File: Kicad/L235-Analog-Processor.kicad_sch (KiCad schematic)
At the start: 300 parts, among them J1 Input A, J10 Half Wave A + -B, J11 Inverted Out B, J12 CV Select, J13 CV Select, J14 Conn_01x20_Pin, J15 Inverted Out A, J16 Full-Wave Rectifier A, J17 Half-Wave Rectifier A, J18 √(A²+B²), J19 Conn_01x20_Socket, J2 Input B, J3 Function IN, J4 ( 10A / |B| ) / ( A * B / 10 ), J5 Output F(x), J6 Power, J7 Full-Wave Rectifier B, J8 A - B, J9 Negative Half-Wave Rectifier B, U1 TL082, U10 TL082, U11 TL082, U12 TL082, U13 TL084, U14 RC4580, U15 TL082, U16 AD633ARZ-RL, U17 TL082, U18 LM4040DBZ-10, U19 74HC148, U2 TL082, U20 LM339, U21 LM339, U22 DG4051E, U23 DG4051E, U24 DG4051E, U25 DG4051E, U26 DG4051E, U27 74LS151, U28 DG4051E, U29 LM339, U3 TL082, U30 LM339, U31 74HC148, U32 DG4051E, U33 DG4051E, U34 DG4051E, U35 DG4051E, U36 LM78M05_TO252, U37 TL082, U4 TL082, U5 TL082, U6 TL082, U7 TL082, U8 TL082, U9 TL082

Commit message: changed diode footprints to SOT-123
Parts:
- added C79, C83: 100nF, Capacitor_SMD:C_0402_1005Metric, symbol Device:C
- added U38: LM13700, symbol Amplifier_Operational:LM13700
- D1, D10, D11, D12, D13, D14, D15, D16, D17, D18, D19, D2, D20, D21, D22, D23, D25, D26, D29, D3, D30, D31, D32, D4, D5, D6, D7, D8, D9: footprint Diode_SMD:D_0402_1005Metric -> Diode_SMD:D_SOD-123
- R35, R37, R38, R82, R87, R88, R89, R91, R92, R93: value 180 -> 1k
- U22, U23, U24, U25, U26, U28: value DG4051E -> CD4051
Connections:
- net +12V: now also C79.1, U38.11 (V+)
- net -12V: now also C83.2, U38.6 (V-)
- net GND: now also TR2.4, C79.2, C83.1
- net at R33.2, RV3.1: no longer TR2.4

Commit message: Added test run
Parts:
- U27: value 74LS151 -> CD4051
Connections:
- net 10V REF is gone; now on net +5V: C43.2, J1.TN, J14.14 (Pin_14), J19.14 (Pin_14), J2.TN, R110.2, R16.2, R2.2, R65.2, R98.2, U18.1 (K)
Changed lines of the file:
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@@
     )
   )
+  (symbol (lib_id "power:+5V") (at 38.1 467.36 0) (unit 1)
+    (in_bom yes) (on_board yes) (dnp no) (fields_autoplaced)
+    (property "Reference" "#PWR0187" (at 38.1 471.17 0)
+      (effects (font (size 1.27 1.27)) hide)
+    )
+    (property "Value" "+5V" (at 38.1 462.28 0)
+      (effects (font (size 1.27 1.27)))
+    )
+    (property "Footprint" "" (at 38.1 467.36 0)
+      (effects (font (size 1.27 1.27)) hide)
+    )
+    (property "Datasheet" "" (at 38.1 467.36 0)
+      (effects (font (size 1.27 1.27)) hide)
+    )
+    (pin "1")
+    (instances
+      (project "L235-Analog-Processor"
+        (path "/11565f7a-671a-4a91-8d3b-c6d6401f938b"
+          (reference "#PWR0187") (unit 1)
+        )
+      )
+    )
+  )
   (symbol (lib_id "Amplifier_Operational:TL082") (at 101.473 266.319 0) (mirror x) (unit 2)
     (in_bom yes) (on_board yes) (dnp no)
@@
       (effects (font (size 1.27 1.27)))
     )
-    (property "Value" "74LS151" (at 181.61 845.9821 0)
+    (property "Value" "CD4051" (at 181.61 845.9821 0)
       (effects (font (size 1.27 1.27)))
     )

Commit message: Added leds selectors
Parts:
- removed H2: MountingHole, MountingHole:MountingHole_3.2mm_M3_DIN965, symbol Mechanical:MountingHole
- added C84, C85, C86, C87: 100nF, Capacitor_SMD:C_0402_1005Metric, symbol Device:C
- added D27, D28, D35, D36, D37, D38, D39, D40, D41, D42, D43, D44, D45: LED, LED_THT:LED_D1.8mm_W3.3mm_H2.4mm, symbol Device:LED
- added J20, J22: Conn_01x05_Socket, Connector_PinHeader_2.54mm:PinHeader_1x05_P2.54mm_Vertical, symbol Connector:Conn_01x05_Socket
- added J21, J23: Conn_01x05_Pin, Connector_PinSocket_2.54mm:PinSocket_1x05_P2.54mm_Vertical, symbol Connector:Conn_01x05_Pin
- added R115, R55: 1k, Resistor_SMD:R_0402_1005Metric, symbol Device:R
- added U39, U40: CD4051, Package_SO:TSSOP-16-1EP_4.4x5mm_P0.65mm_EP3x3mm, symbol 4xxx:4051
- RV7: value 500k -> 1M Log
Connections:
- net +12V: now also C84.2, C87.2, U39.16 (VDD), U40.16 (VDD)
- net +5V: now also J20.5 (Pin_5), J21.5 (Pin_5), J22.5 (Pin_5), J23.5 (Pin_5), R115.1, R55.1; no longer C43.2, J1.TN, J14.14 (Pin_14), J19.14 (Pin_14), J2.TN, R2.2, U18.1 (K)
- net -12V: now also C85.2, C86.2, U39.8 (VSS), U40.8 (VSS)
- net A0: now also J20.2 (Pin_2), J21.2 (Pin_2), U39.11 (A)
- net A1: now also J20.3 (Pin_3), J21.3 (Pin_3), U39.10 (B)
- net A2: now also J20.4 (Pin_4), J21.4 (Pin_4), U39.9 (C)
- net B0: now also J22.2 (Pin_2), J23.2 (Pin_2), U40.11 (A)
- net B1: now also J22.3 (Pin_3), J23.3 (Pin_3), U40.10 (B)
- net B2: now also J22.4 (Pin_4), J23.4 (Pin_4), U40.9 (C)
- net GND: now also C84.1, C85.1, C86.1, C87.1, D27.1 (K), D28.1 (K), D35.1 (K), D36.1 (K), D37.1 (K), D38.1 (K), D39.1 (K), D40.1 (K), D41.1 (K), D42.1 (K), D43.1 (K), D44.1 (K), D45.1 (K), J20.1 (Pin_1), J21.1 (Pin_1), J22.1 (Pin_1), J23.1 (Pin_1), U39.6 (Inh), U39.7 (VEE), U40.6 (Inh), U40.7 (VEE)
- new net: R55.2, U40.3 (X)
- new net: R115.2, U39.3 (X)
- new net 10V REF: C43.2, J1.TN, J14.14 (Pin_14), J19.14 (Pin_14), J2.TN, R2.2, U18.1 (K)
- new net LED_A1: D27.2 (A), U39.13 (X0)
- new net LED_A2: D28.2 (A), U39.14 (X1)
- new net LED_A3: D35.2 (A), U39.15 (X2)
- new net LED_A4: D39.2 (A), U39.12 (X3)
- new net LED_A5: D38.2 (A), U39.1 (X4)
- new net LED_A6: D37.2 (A), U39.5 (X5)
- new net LED_A7: D36.2 (A), U39.2 (X6)
- new net LED_B1: D40.2 (A), U40.13 (X0)
- new net LED_B2: D41.2 (A), U40.14 (X1)
- new net LED_B3: D42.2 (A), U40.15 (X2)
- new net LED_B4: D43.2 (A), U40.12 (X3)
- new net LED_B5: D44.2 (A), U40.1 (X4)
- new net LED_B6: D45.2 (A), U40.5 (X5)
- no-connect marks 52 -> 55
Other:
- note added: "( 10A / |B| ) / ( A * B / 10 )"
- note added: "A"
- note added: "B"
- note added: "Integrator"
- note added: "Negative"
- note added: "ln |X| / √|X| / X²"

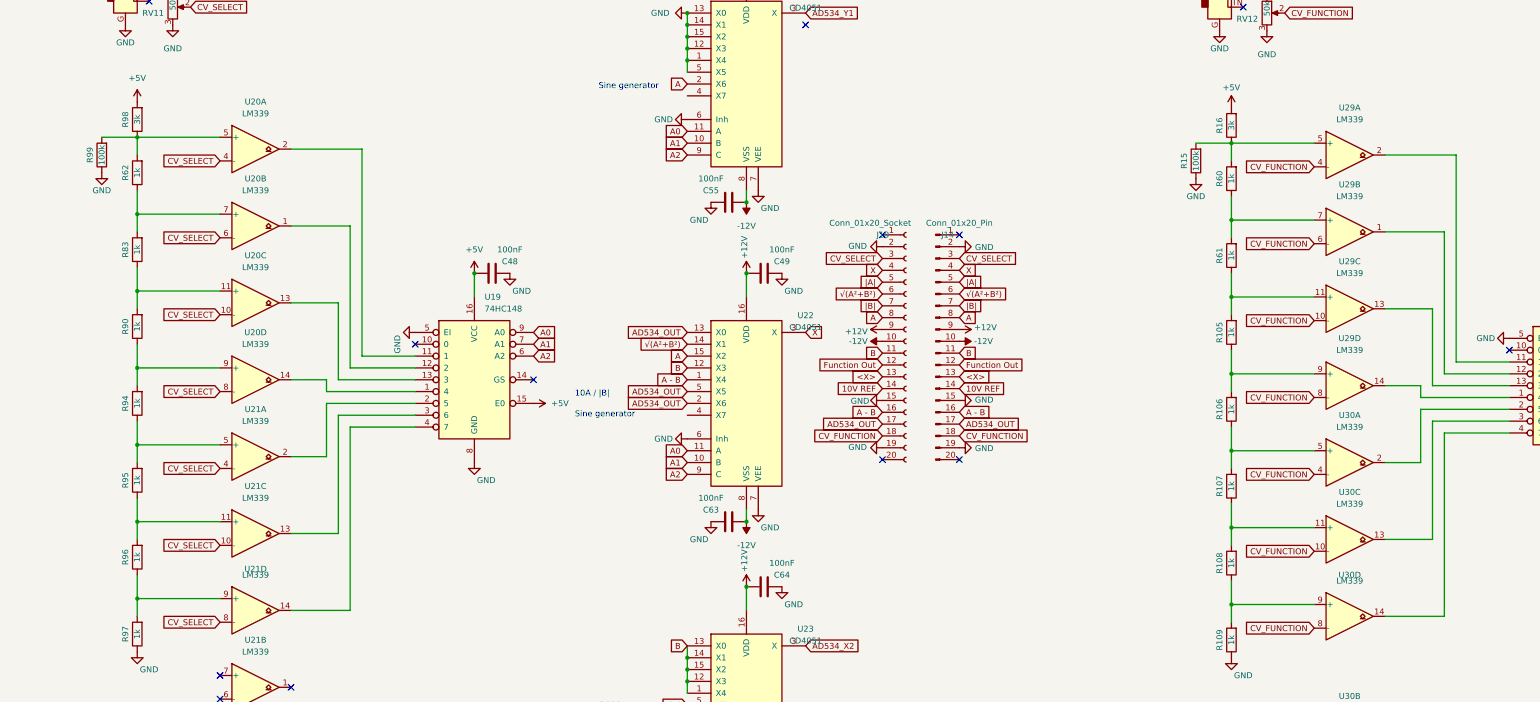
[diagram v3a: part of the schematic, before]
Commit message: Added missing Vlogic to comparators
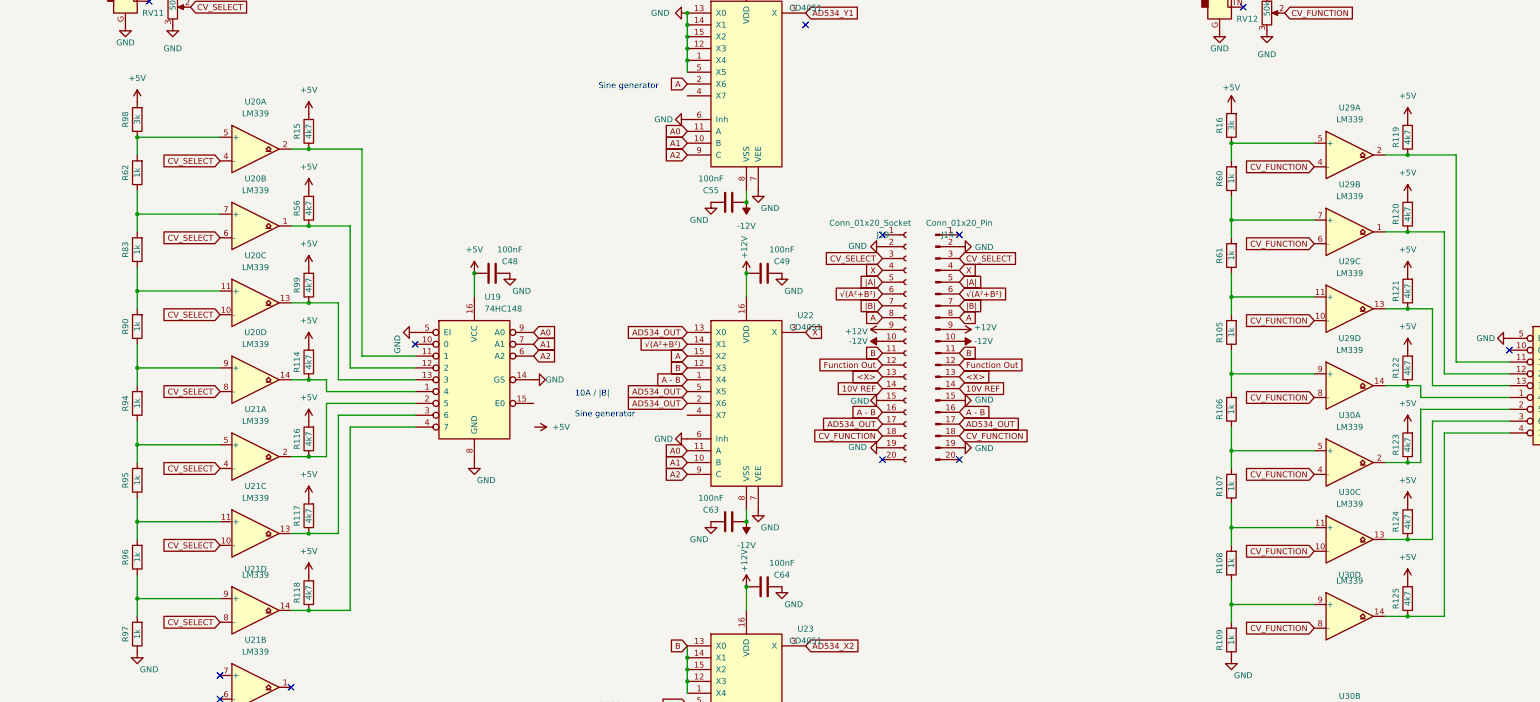
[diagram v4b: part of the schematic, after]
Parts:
- added R114, R116, R117, R118, R119, R120, R121, R122, R123, R124, R125, R56: 4k7, Resistor_SMD:R_0402_1005Metric, symbol Device:R
- R15, R99: value 100k -> 4k7
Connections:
- net +5V: now also R15.2, R99.2, R114.2, R116.2, R117.2, R118.2, R119.2, R120.2, R121.2, R122.2, R123.2, R124.2, R125.2, R56.2; no longer U19.15 (E0)
- net GND: now also U19.14 (GS); no longer R15.1, R99.1
- net at R62.2, R98.1, U20.5 (+): no longer R99.2
- net at U29.1, U31.12 (2): now also R120.1
- net at U19.2 (5), U21.2: now also R116.1
- net at U30.14, U31.4 (7): now also R125.1
- net at R16.1, R60.2, U29.5 (+): no longer R15.2
- net at U29.13, U31.13 (3): now also R121.1
- net at U29.14, U31.1 (4): now also R122.1
- net at U29.2, U31.11 (1): now also R119.1
- net at U19.11 (1), U20.2: now also R15.1
- net at U19.13 (3), U20.13: now also R99.1
- net at U30.2, U31.2 (5): now also R123.1
- net at U30.13, U31.3 (6): now also R124.1
- net at U19.1 (4), U20.14: now also R114.1
- net at U19.4 (7), U21.14: now also R118.1
- net at U19.12 (2), U20.1: now also R56.1
- net at U19.3 (6), U21.13: now also R117.1
- no-connect marks 55 -> 54

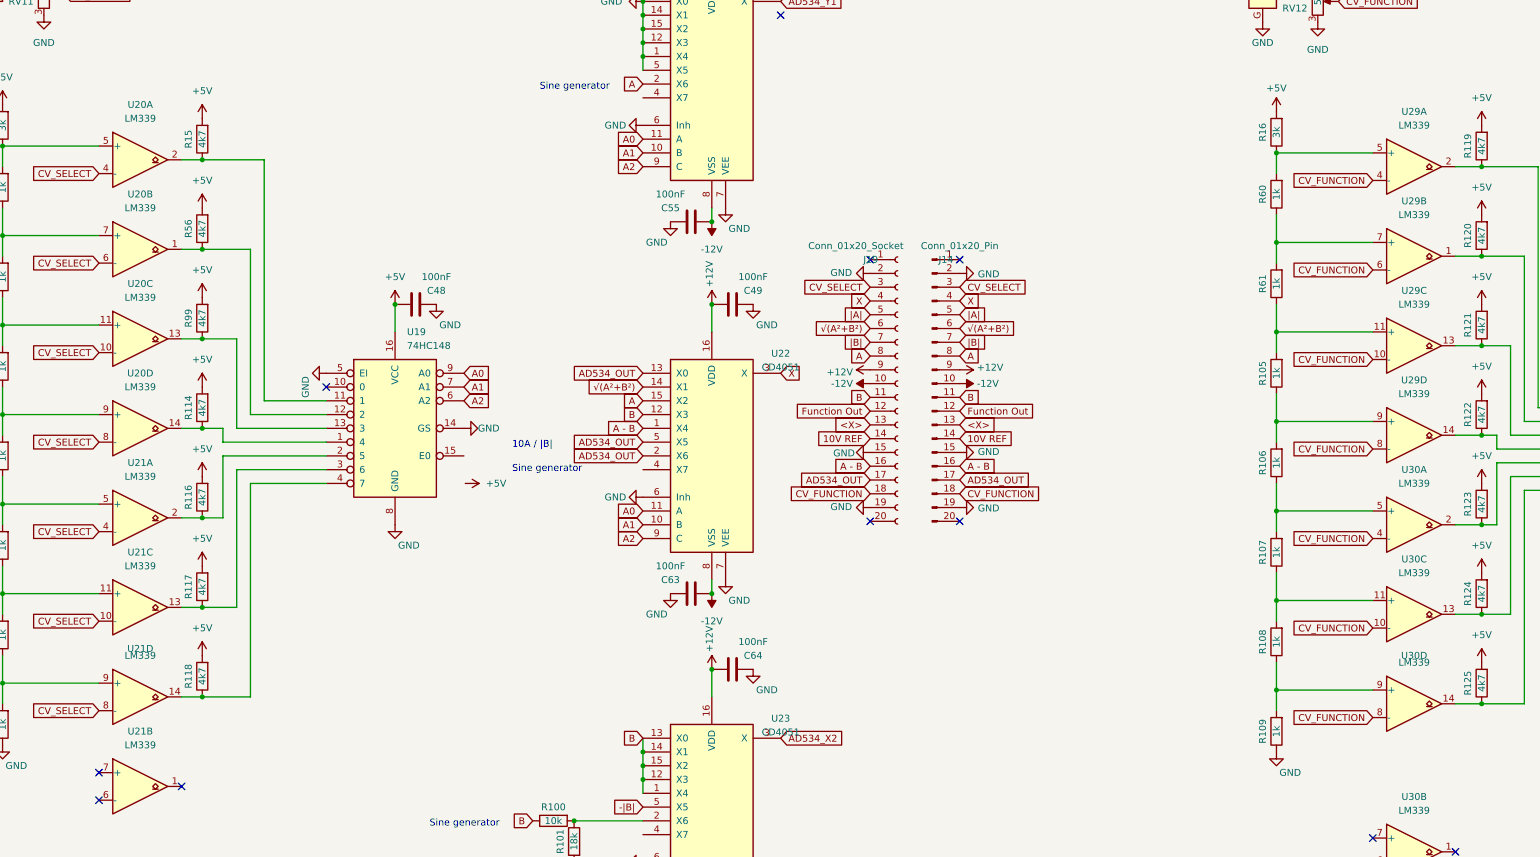
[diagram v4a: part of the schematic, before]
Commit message: Flipped +- comparators to fix H/L order to actually work with logic table
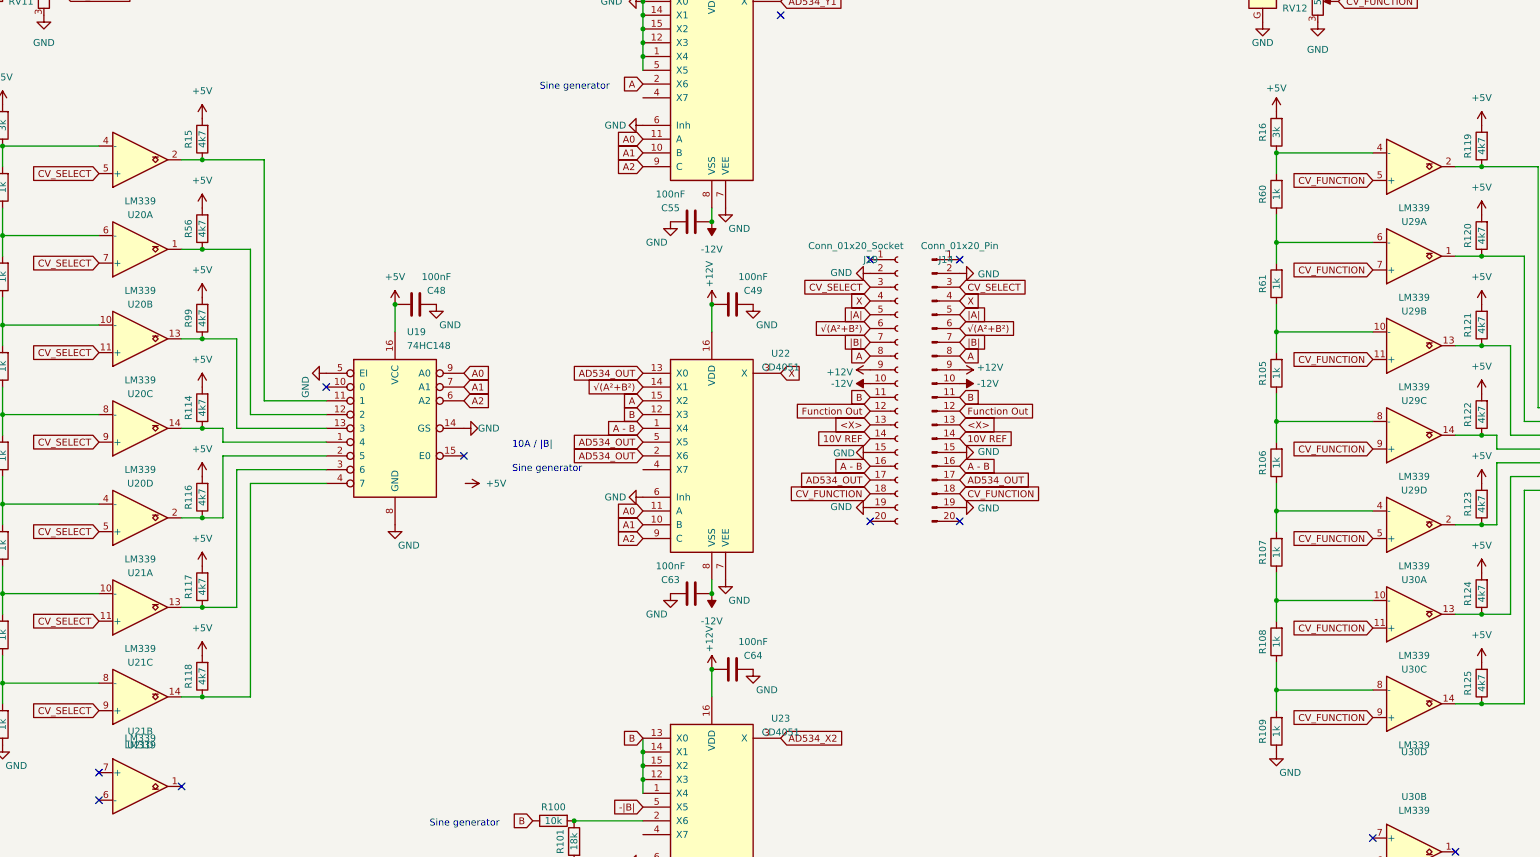
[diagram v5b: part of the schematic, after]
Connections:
- net CV_FUNCTION: now also U29.11 (+), U29.5 (+), U29.7 (+), U29.9 (+), U30.11 (+), U30.5 (+), U30.9 (+); no longer U29.10 (-), U29.4 (-), U29.6 (-), U29.8 (-), U30.10 (-), U30.4 (-), U30.8 (-)
- net CV_SELECT: now also U20.11 (+), U20.5 (+), U20.7 (+), U20.9 (+), U21.11 (+), U21.5 (+), U21.9 (+); no longer U20.10 (-), U20.4 (-), U20.6 (-), U20.8 (-), U21.10 (-), U21.4 (-), U21.8 (-)
- net at R62.2, R98.1: now also U20.4 (-); no longer U20.5 (+)
- net at R60.1, R61.2: now also U29.6 (-); no longer U29.7 (+)
- net at R94.1, R95.2: now also U21.4 (-); no longer U21.5 (+)
- net at R90.1, R94.2: now also U20.8 (-); no longer U20.9 (+)
- net at R108.1, R109.2: now also U30.8 (-); no longer U30.9 (+)
- net at R107.1, R108.2: now also U30.10 (-); no longer U30.11 (+)
- net at R16.1, R60.2: now also U29.4 (-); no longer U29.5 (+)
- net at R95.1, R96.2: now also U21.10 (-); no longer U21.11 (+)
- net at R105.2, R61.1: now also U29.10 (-); no longer U29.11 (+)
- net at R105.1, R106.2: now also U29.8 (-); no longer U29.9 (+)
- net at R83.1, R90.2: now also U20.10 (-); no longer U20.11 (+)
- net at R62.1, R83.2: now also U20.6 (-); no longer U20.7 (+)
- net at R96.1, R97.2: now also U21.8 (-); no longer U21.9 (+)
- net at R106.1, R107.2: now also U30.4 (-); no longer U30.5 (+)
- no-connect marks 54 -> 55

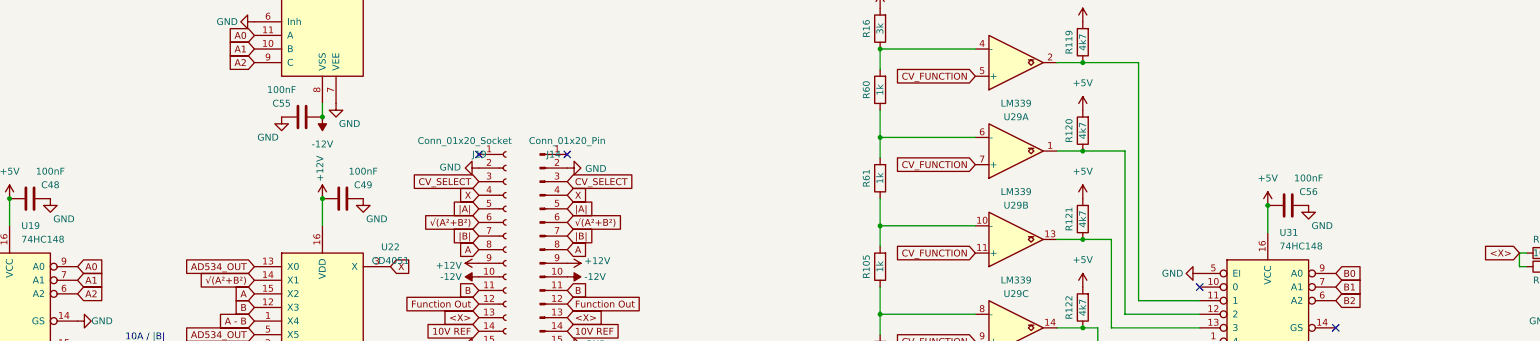
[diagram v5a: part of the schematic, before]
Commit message: Cleanup trace thickness, text alignment
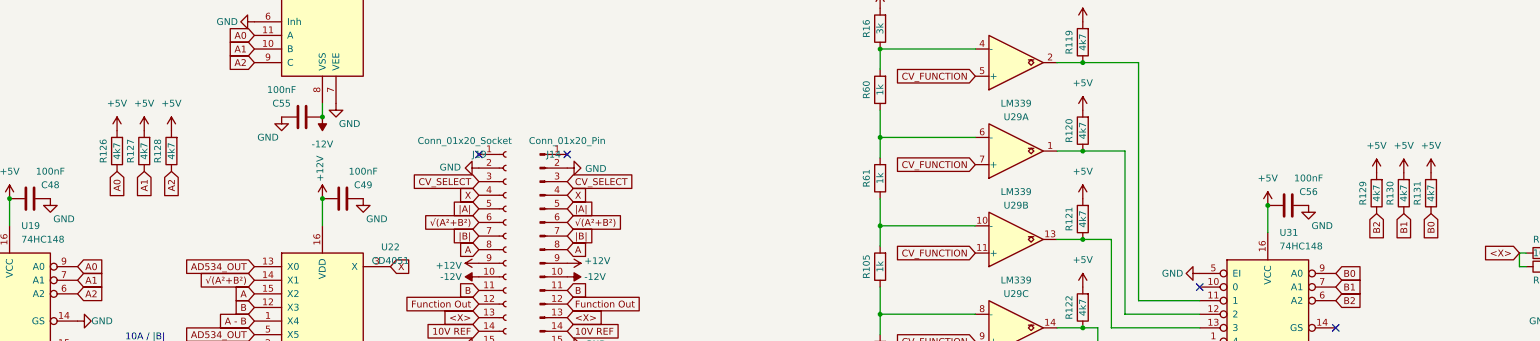
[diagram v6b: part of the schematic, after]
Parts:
- added R126, R127, R128, R129, R130, R131: 4k7, Resistor_SMD:R_0402_1005Metric, symbol Device:R
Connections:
- net +5V: now also R126.2, R127.2, R128.2, R129.2, R130.2, R131.2
- net A0: now also R126.1
- net A1: now also R127.1
- net A2: now also R128.1
- net B0: now also R131.1
- net B1: now also R130.1
- net B2: now also R129.1

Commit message: Removed invert jacks for attenuverter + offset knob
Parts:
- removed C43, C79, C83: 100nF, Capacitor_SMD:C_0402_1005Metric, symbol Device:C
- removed J11: Inverted Out B, Custom_Footprints:Cliff_3.5mm_Stereo_Jack, symbol Connector_Audio:AudioJack2_Ground_SwitchT
- removed J15: Inverted Out A, Custom_Footprints:Cliff_3.5mm_Stereo_Jack, symbol Connector_Audio:AudioJack2_Ground_SwitchT
- removed U18: LM4040DBZ-10, Package_TO_SOT_SMD:SOT-23, symbol Reference_Voltage:LM4040DBZ-10
- removed U38: LM13700, symbol Amplifier_Operational:LM13700
- added R132, R135, R138: 100k, Resistor_SMD:R_0402_1005Metric, symbol Device:R
- added R133, R134: 47k, Resistor_SMD:R_0402_1005Metric, symbol Device:R
- added R137: 220k, Resistor_SMD:R_0402_1005Metric, symbol Device:R
- added RV13, RV15: 100k, Potentiometer_THT:Potentiometer_Alpha_RD901F-40-00D_Single_Vertical, symbol Device:R_Potentiometer
- R1, R3, R4, R84: value 10k -> 100k
- R2: value 1k -> 220k
- R39: value 10k -> 47k
- R82: value 1k -> 47k
- R87: value 1k -> 100k
- U15: footprint Package_SO:SO-8_3.9x4.9mm_P1.27mm -> Package_SO:SOIC-8_3.9x4.9mm_P1.27mm
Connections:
- net +12V: now also U15.4 (V-), RV13.3, RV15.3; no longer R2.1, U15.8 (V+)
- net -12V: now also U15.8 (V+), RV13.1, RV15.1; no longer U15.4 (V-)
- net A: now also R87.2, U1.7; no longer R84.1, U1.1, U1.2 (-), U15.2 (-)
- net B: now also U15.7, R138.2; no longer R4.1, U1.6 (-), U1.7
- net GND: now also J1.TN, J2.TN, U1.5 (+); no longer U15.3 (+)
- net at R82.1: now also RV10.2
- net at R4.2, U15.6 (-): now also R137.2, R138.1; no longer R39.1
- net at J2.T, RV10.1: now also R3.1, R39.2
- net at R3.2: now also R84.1, U15.2 (-); no longer U1.5 (+)
- net at U1.3 (+): now also R133.1, R134.2; no longer R1.2
- net at J1.T, RV9.1: now also R1.2, R133.2
- net at R1.1: now also U1.2 (-), R132.1; no longer RV9.2
- net at R87.1: now also R2.2, U1.6 (-), R135.2
- net -A: no longer names the net of R84.2, U15.1
- net -A: now also R4.1; no longer R87.2
- removed net -B: R39.2, R82.2, U15.7
- removed net 10V REF: J1.TN, J14.14 (Pin_14), J19.14 (Pin_14), J2.TN, R2.2
- new net: R39.1, R82.2, U15.3 (+)
- new net: R137.1, RV15.2
- new net: R132.2, R135.1, U1.1
- new net: R134.1, RV9.2
- new net: R2.1, RV13.2
- no-connect marks 55 -> 53
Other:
- note added: "Attenuverter & Offset input A"
- note added: "Attenuverter & Offset input B"
- note removed: "10V REF"
- note removed: "Buffered input A"
- note removed: "Buffered input B"
- note removed: "Invert A"
- note removed: "Invert B"
- moved on the sheet: J1, J14, J19, J2, R1, R3, RV10, RV9, U1A, U1B
